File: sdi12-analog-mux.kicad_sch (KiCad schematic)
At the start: 117 parts, among them J1 Conn_01x02, J10 Screw_Terminal_01x04, J11 Screw_Terminal_01x04, J12 Screw_Terminal_01x04, J2 USB_B_Micro, J3 SM03B-SRSS-TB, J4 Screw_Terminal_01x03, J5 Conn_01x03_Socket, J6 Screw_Terminal_01x04, J7 Screw_Terminal_01x04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

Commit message: ordered boards v0.0 and started CAD
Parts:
- C11, C22, C54: footprint Capacitor_SMD:C_0805_2012Metric -> Capacitor_SMD:C_0402_1005Metric
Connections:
- net MUX_A0: now also U7.32 (GPIO21); no longer U7.5 (GPIO3)
- net MUX_A1: now also U7.34 (GPIO22); no longer U7.6 (GPIO4)
- net MUX_A2: now also U7.35 (GPIO23); no longer U7.7 (GPIO5)
- net MUX_EN: now also U7.31 (GPIO20); no longer U7.4 (GPIO2)
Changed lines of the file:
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@@
 		)
 	)
-	(label "MUX_A1"
-		(at 217.17 92.71 0)
-		(effects
-			(font
-				(size 1.27 1.27)
-			)
-			(justify left bottom)
-		)
-	)
 	(label "SDI12_DATA_3V3"
 		(at 119.38 229.87 180)
@@
 		)
 	)
+	(label "MUX_A2"
+		(at 217.17 140.97 0)
+		(effects
+			(font
+				(size 1.27 1.27)
+			)
+			(justify left bottom)
+		)
+	)
 	(label "SCLK"
 		(at 217.17 128.27 0)
@@
 		)
 	)
+	(label "MUX_A1"
+		(at 217.17 138.43 0)
+		(effects
+			(font
+				(size 1.27 1.27)
+			)
+			(justify left bottom)
+		)
+	)
 	(label "USB_D-"
 		(at 48.26 149.86 180)
@@
 		)
 	)
+	(label "MUX_EN"
+		(at 217.17 133.35 0)
+		(effects
+			(font
+				(size 1.27 1.27)
+			)
+			(justify left bottom)
+		)
+	)
 	(label "~{USB_BOOT}"
 		(at 27.94 52.07 0)
@@
 		)
 	)
-	(label "MUX_EN"
-		(at 217.17 87.63 0)
-		(effects
-			(font
-				(size 1.27 1.27)
-			)
-			(justify left bottom)
-		)
-	)
 	(label "RTD_6_POS"
 		(at 251.46 143.51 180)
@@
 		)
 	)
-	(label "MUX_A2"
-		(at 217.17 95.25 0)
-		(effects
-			(font
-				(size 1.27 1.27)
-			)
-			(justify left bottom)
-		)
-	)
 	(label "QSPI_SD3"
 		(at 67.31 64.77 0)
@@
 	)
 	(label "MUX_A0"
-		(at 217.17 90.17 0)
+		(at 217.17 135.89 0)
 		(effects
 			(font
@@
 			)
 		)
-		(property "Footprint" "Capacitor_SMD:C_0805_2012Metric"
+		(property "Footprint" "Capacitor_SMD:C_0402_1005Metric"
 			(at 234.6452 270.51 0)
 			(effects
@@
 			)
 		)
-		(property "Footprint" "Capacitor_SMD:C_0805_2012Metric"
+		(property "Footprint" "Capacitor_SMD:C_0402_1005Metric"
 			(at 388.62 175.26 0)
 			(effects
@@
 			)
 		)
-		(property "Footprint" "Capacitor_SMD:C_0805_2012Metric"
+		(property "Footprint" "Capacitor_SMD:C_0402_1005Metric"
 			(at 127.9652 275.59 0)
 			(effects

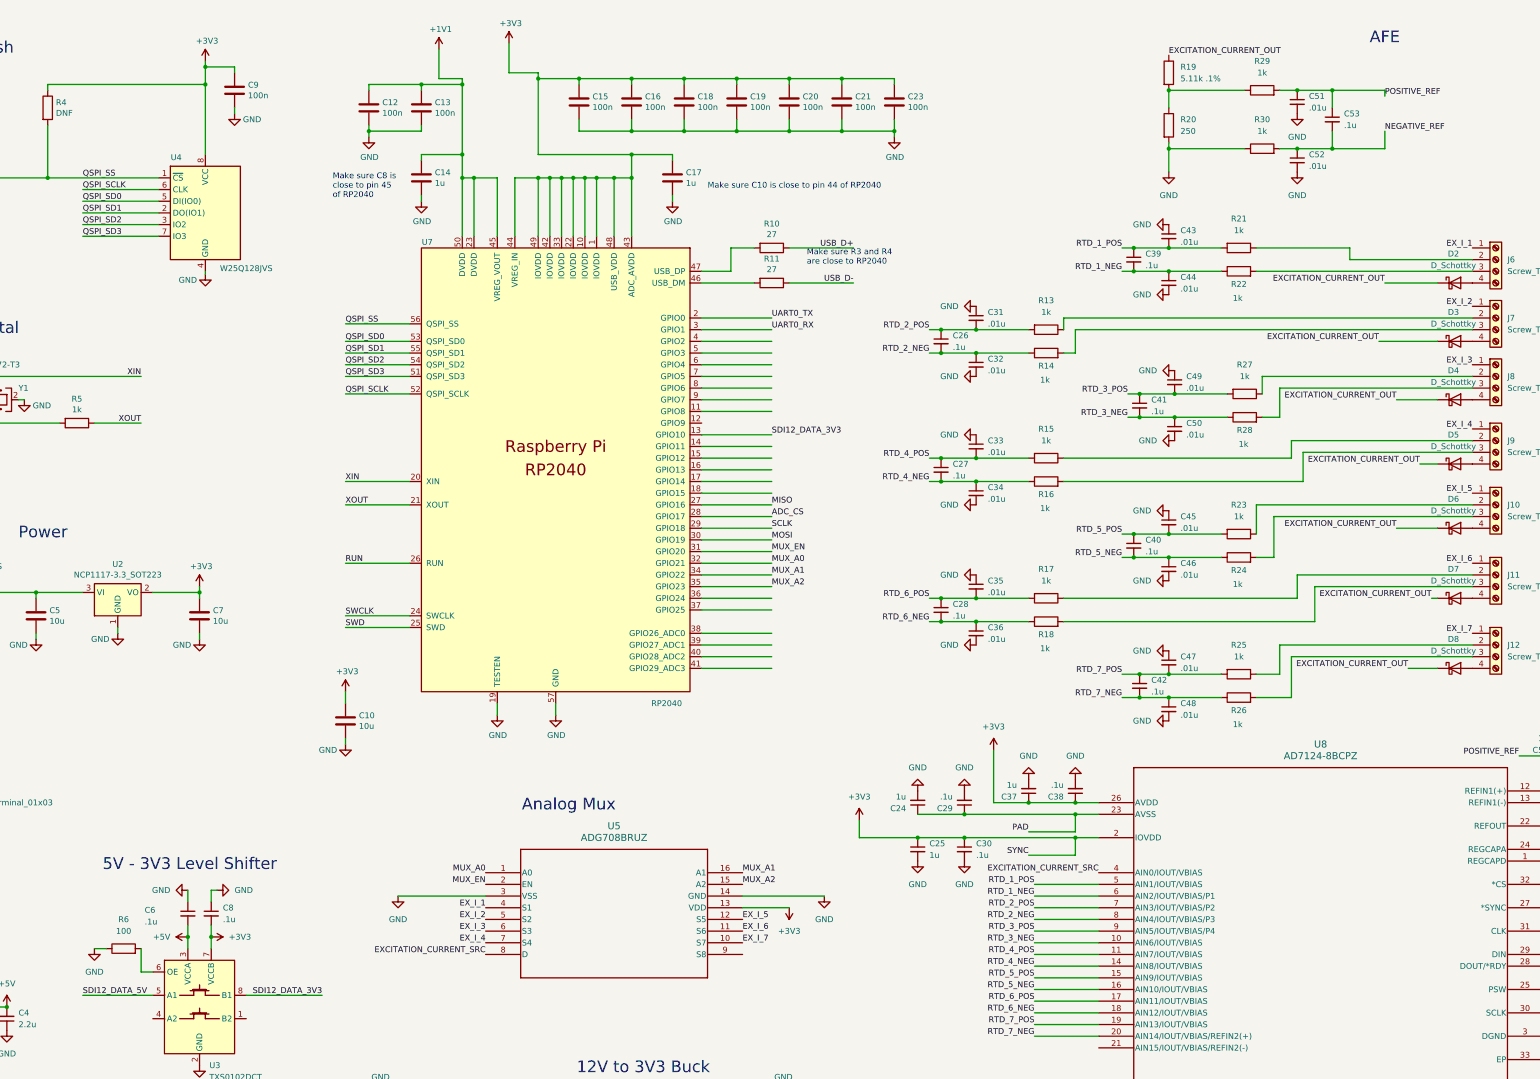
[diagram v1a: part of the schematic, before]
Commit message: version 1.0 after v0.0 bringup modifications
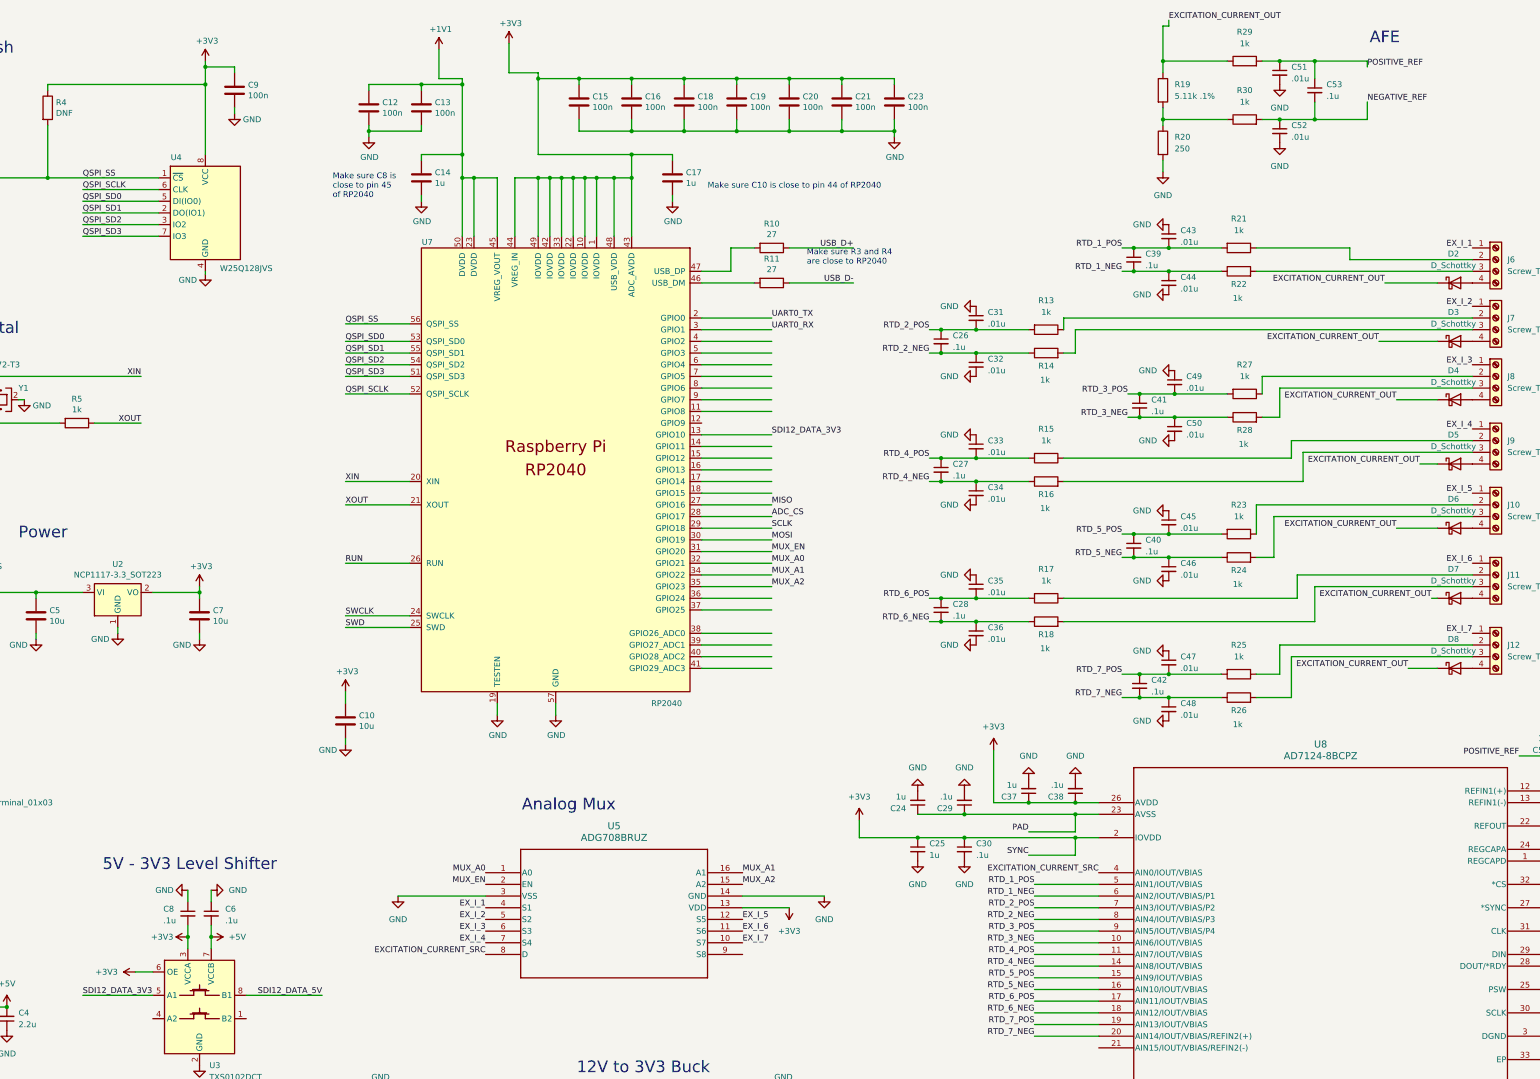
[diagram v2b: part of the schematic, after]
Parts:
- removed R6: 100, Resistor_SMD:R_0402_1005Metric, symbol Device:R
- D2, D3, D4, D5, D6, D7, D8: footprint Diode_SMD:D_0402_1005Metric -> Diode_SMD:D_SOD-323F
- L1: footprint Capacitor_SMD:C_0402_1005Metric -> 74438334022:WE-MAPI_3012
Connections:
- net +3V3: now also U3.3 (VCCA), U3.6 (OE); no longer U3.7 (VCCB)
- net +5V: now also U3.7 (VCCB); no longer U3.3 (VCCA)
- net EXCITATION_CURRENT_OUT: now also R29.1
- net GND: no longer R30.1
- net SDI12_DATA_3V3: now also U3.5 (A1); no longer U3.8 (B1)
- net SDI12_DATA_5V: now also U3.8 (B1); no longer U3.5 (A1)
- net at R19.2, R20.1: now also R30.1; no longer R29.1
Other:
- moved on the sheet: C51, C52, C53, C6, C8, R19, R20, R29, R30
